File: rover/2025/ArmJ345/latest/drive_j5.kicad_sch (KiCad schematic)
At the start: 9 parts, among them J1 XT30PW-F, U1 IFX9201SGAUMA1

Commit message: .
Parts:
- C2: value 100uF -> 470uF; footprint Capacitor_SMD:CP_Elec_6.3x7.7 -> Capacitor_SMD:CP_Elec_8x10.5
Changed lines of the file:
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@@
 			)
 		)
-		(property "Value" "100uF"
+		(property "Value" "470uF"
 			(at 39.37 41.0209 0)
 			(effects
@@
 			)
 		)
-		(property "Footprint" "Capacitor_SMD:CP_Elec_6.3x7.7"
+		(property "Footprint" "Capacitor_SMD:CP_Elec_8x10.5"
 			(at 36.5252 44.45 0)
 			(effects
@@
 			)
 		)
-		(property "Description" "865080545012"
+		(property "Description" "UCV1V471MNL1GS"
 			(at 35.56 40.64 0)
 			(effects

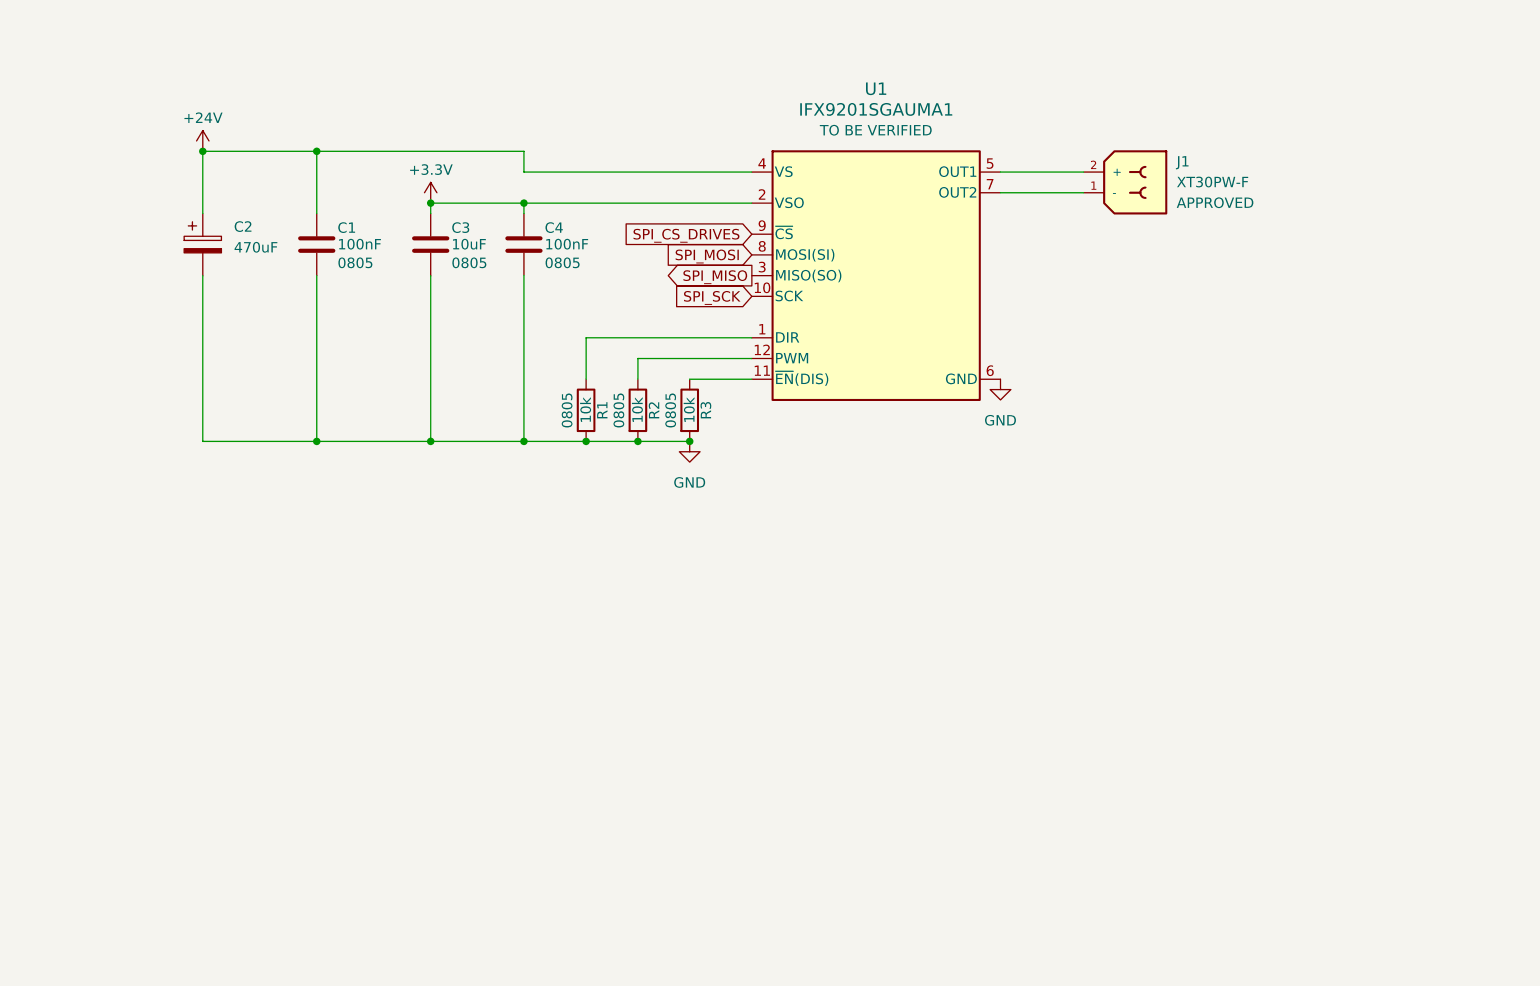
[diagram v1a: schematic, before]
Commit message: ArmJ345 routing
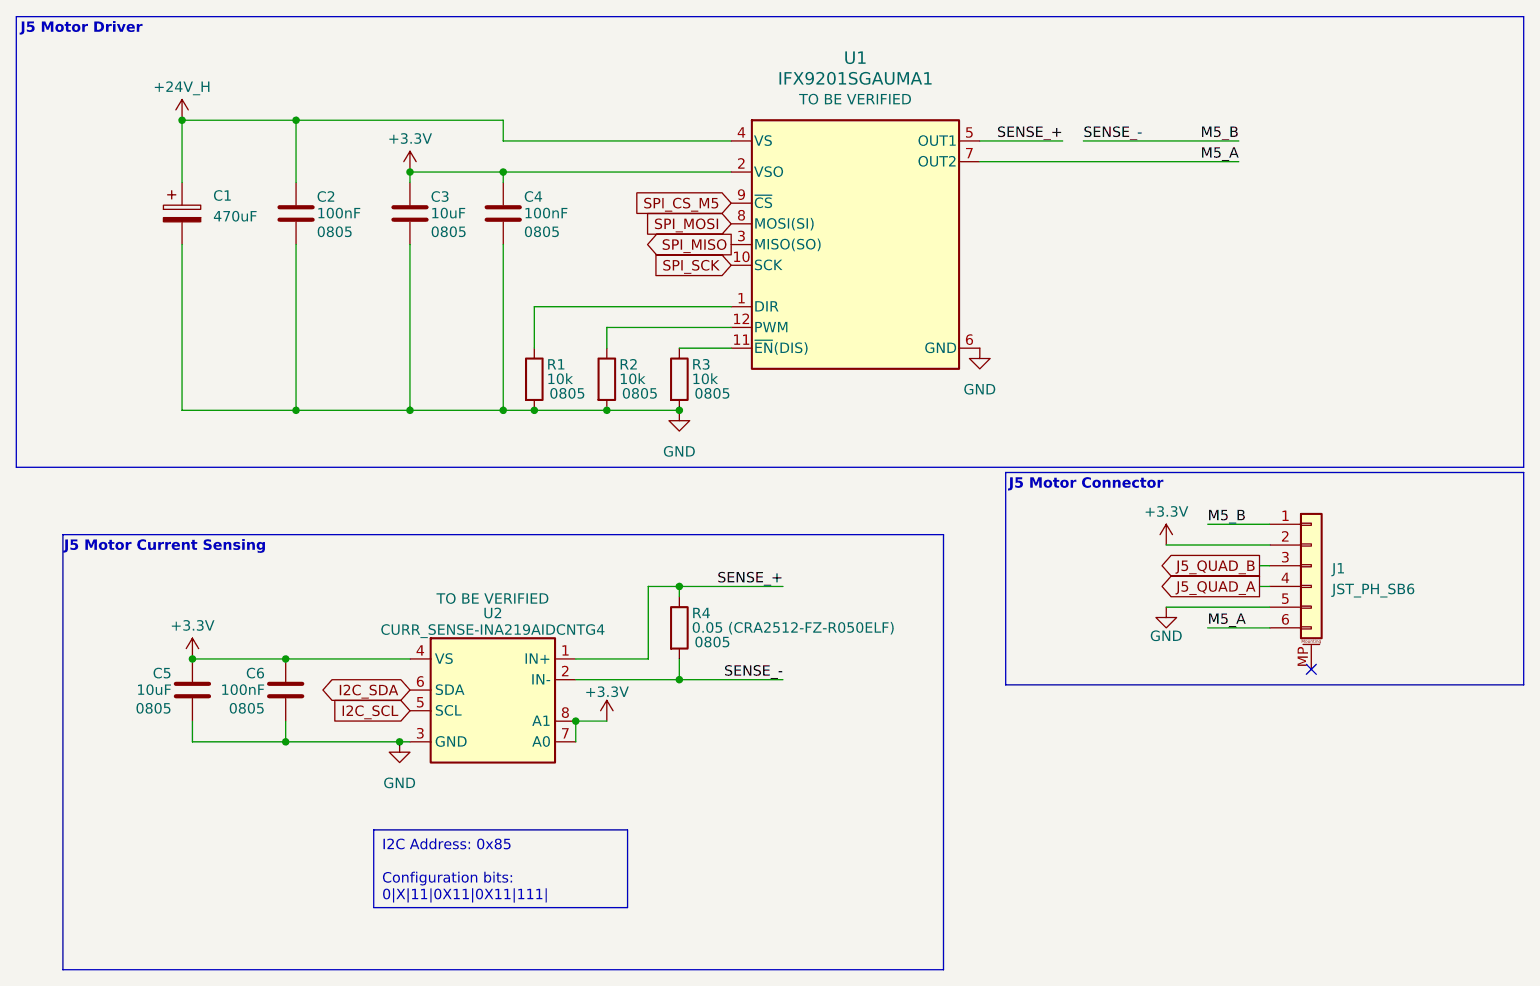
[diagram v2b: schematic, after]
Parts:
- removed J1: XT30PW-F, RoverFootprint:AMASS_XT30PW-F_1x02_P2.50mm_Horizontal, symbol RoverLibrary:XT30PW-F
- added C5: 10uF, Capacitor_SMD:C_0805_2012Metric_Pad1.18x1.45mm_HandSolder, symbol RoverLibrary:C_0805
- added C6: 100nF, Capacitor_SMD:C_0805_2012Metric_Pad1.18x1.45mm_HandSolder, symbol RoverLibrary:C_0805
- added J1: JST_PH_SB6, Connector_JST:JST_PH_S6B-PH-SM4-TB_1x06-1MP_P2.00mm_Horizontal, symbol Connector_Generic_MountingPin:Conn_01x06_MountingPin
- added R4: 0.05 (CRA2512-FZ-R050ELF), Resistor_SMD:R_2512_6332Metric_Pad1.40x3.35mm_HandSolder, symbol RoverLibrary:R_0805
- added U2: CURR_SENSE-INA219AIDCNTG4, Package_TO_SOT_SMD:SOT-23-8, symbol RoverLibrary:CURR_SENSE-INA219AIDCNTG4
- renumbered C2 to C1, C1 to C2
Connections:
- net +3.3V: now also C5.1, C6.1, J1.2 (Pin_2), U2.4 (VS), U2.7 (A0), U2.8 (A1)
- net GND: now also C5.2, C6.2, J1.5 (Pin_5), U2.3 (GND)
- net M5_A: now reaches U1.7 (OUT2)
- net M5_A: now also J1.6 (Pin_6)
- net SENSE_+: now reaches U1.5 (OUT1)
- net SENSE_+: now also R4.1, U2.1 (IN+)
- net +24V renamed +24V_H
- net SPI_CS_DRIVES renamed SPI_CS_M5
- new net I2C_SCL: U2.5 (SCL)
- new net I2C_SDA: U2.6 (SDA)
- new net J5_QUAD_A: J1.4 (Pin_4)
- new net J5_QUAD_B: J1.3 (Pin_3)
- new net M5_B: J1.1 (Pin_1), R4.2, U2.2 (IN-)
- no-connect marks 0 -> 1
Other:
- note added: "J5 Motor Connector"
- note added: "J5 Motor Current Sensing"
- note added: "J5 Motor Driver"
- moved on the sheet: C1, C2, C3, C4, R1, U1

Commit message: armj345 fixes
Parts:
- added R33: 10k, Resistor_SMD:R_0805_2012Metric_Pad1.20x1.40mm_HandSolder, symbol RoverLibrary:R_0805
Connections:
- net +3.3V: now also R33.1
- net J5_DIR: now reaches R1.1, U1.1 (DIR)
- net J5_PWM: now reaches R2.1, U1.12 (PWM)
- net SPI_CS_M5: no longer names the net of U1.9 (~{CS})
- net SPI_CS_M5: now also R33.2
- net SPI_MISO: no longer names the net of U1.3 (MISO(SO))
- net SPI_MOSI: no longer names the net of U1.8 (MOSI(SI))
- net SPI_SCK: no longer names the net of U1.10 (SCK)
- no-connect marks 1 -> 4
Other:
- moved on the sheet: C1, C2, C3, C4, R1
